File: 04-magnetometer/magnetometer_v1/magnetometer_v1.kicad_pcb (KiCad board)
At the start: 4 copper layers, 28.5 x 23.5 mm, 42 parts, among them IC1 STM32F072CBT6, IC2 TMAG5170A1QDGKR, IC3 TCAN1042GVDRQ1, J1 Conn_02x04_Odd_Even, J2 USB4110-GF-A, SW3 SW_SPDT, U1 SPX3819M5-L-3-3/TR, U2 NANOT100AS, U3 NANOT100AS

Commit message: clean up routing
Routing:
- net GND: track 75.3 -> 76.1 mm

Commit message: made review changes
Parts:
- moved R4 0.91 mm to (176.4, 64.2), turned to 180 degrees
- moved R8 0.30 mm to (178.0, 65.3)
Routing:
- net GND: track 76.1 -> 68.6 mm, vias 36 -> 33
- net USB_D+: track 12.1 -> 13.9 mm
- net CAN_STM: track 21.4 -> 19.8 mm
- net USB_D-: track 13.3 -> 14.4 mm
- net 5v: track 2.45 -> 3.20 mm
- net 3v3: track 51.9 -> 52.5 mm, vias 11 -> 10

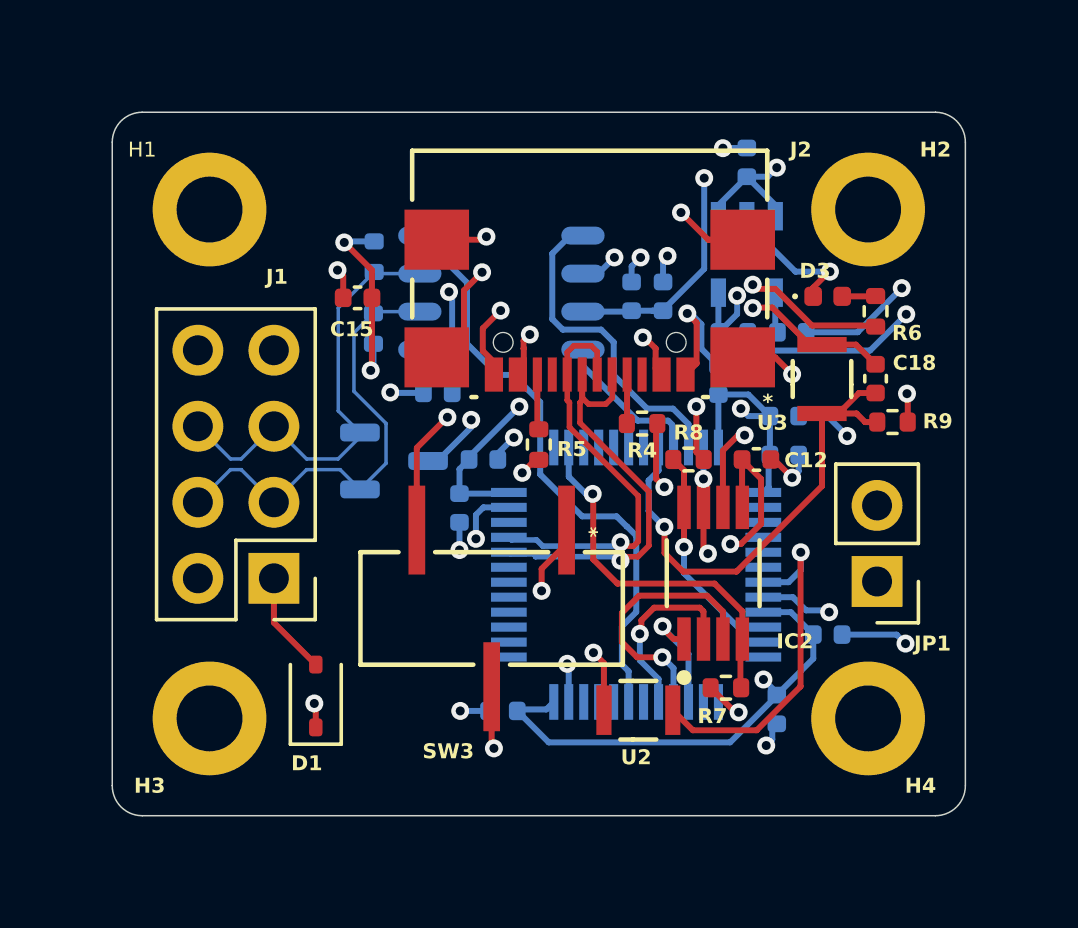
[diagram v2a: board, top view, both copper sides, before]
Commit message: update slide switch footprint
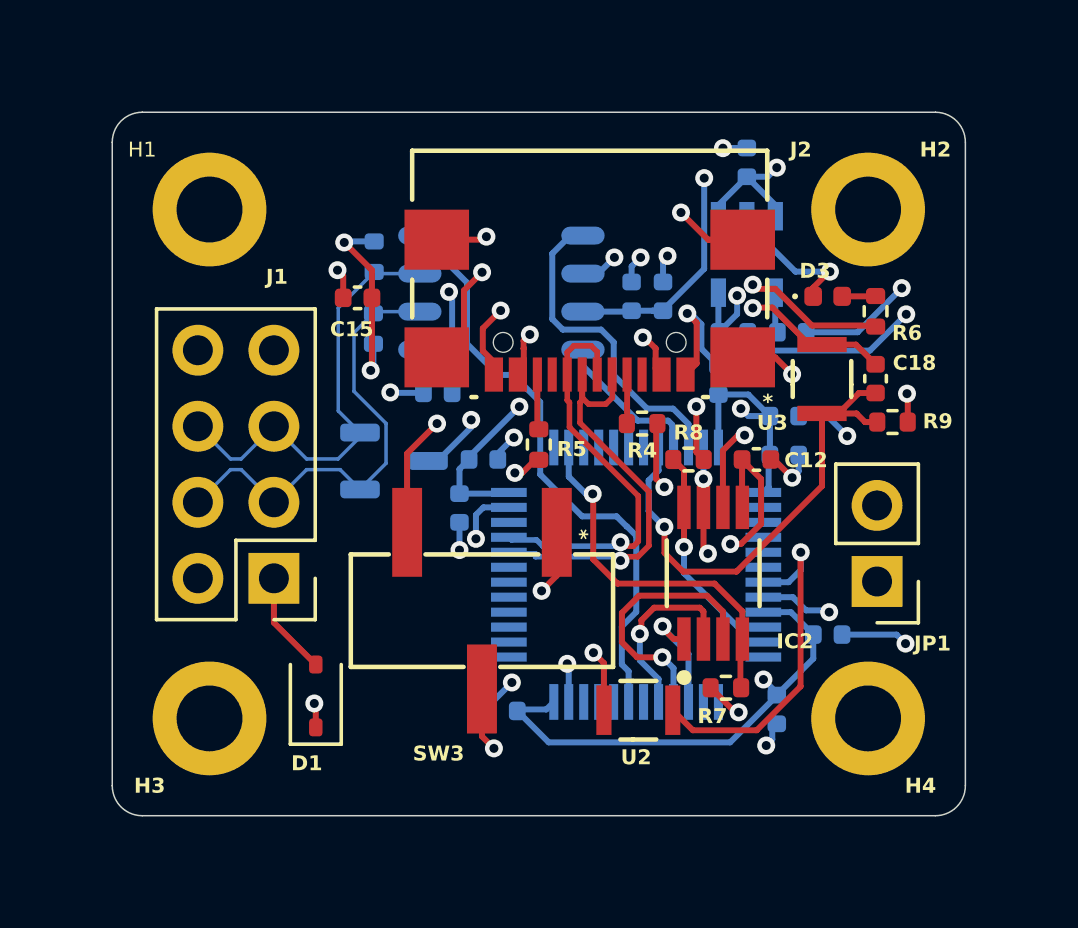
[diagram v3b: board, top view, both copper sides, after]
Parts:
- moved SW3 0.33 mm to (171.1, 70.4)
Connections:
- J2 pad 15: GND -> (no net)
- J2 pad 16: GND -> (no net)
- J2 pad 17: GND -> (no net)
- J2 pad 18: GND -> (no net)
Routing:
- net GND: track 68.6 -> 69.2 mm
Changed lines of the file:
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@@
 	(footprint "mag-fp:SW_JS102011SCQN"
 		(layer "F.Cu")
-		(at 171.425 70.325 -90)
+		(at 171.1 70.4 -90)
 		(tags "JS102011SCQN ")
 		(property "Reference" "SW3"
@@
 		(pad "1" smd rect
 			(at -2.6162 -2.5 270)
-			(size 2.9718 0.5588)
+			(size 2.9718 1)
 			(layers "F.Cu" "F.Mask" "F.Paste")
 			(net 8 "5v")
@@
 		(pad "2" smd rect
 			(at 2.6162 0 270)
-			(size 2.9718 0.5588)
+			(size 2.9718 1)
 			(layers "F.Cu" "F.Mask" "F.Paste")
 			(net 55 "VIN_JUMP")
@@
 		(pad "3" smd rect
 			(at -2.6162 2.5 270)
-			(size 2.9718 0.5588)
+			(size 2.9718 1)
 			(layers "F.Cu" "F.Mask" "F.Paste")
 			(net 52 "VBUS")
@@
 		)
 		(embedded_fonts no)
-		(model "${KICAD9_3DMODEL_DIR}/Package_TO_SOT_SMD.3dshapes/SuperSOT-3.step"
-			(offset
-				(xyz 0 0 0)
-			)
-			(scale
-				(xyz 2.6 2.7 1)
-			)
-			(rotate
-				(xyz -0 -0 -0)
-			)
-		)
 	)
 	(footprint "mag-fp:TMAG5170A2QDGKR"
@@
 			(size 2.159 2.0066)
 			(layers "F.Cu" "F.Mask" "F.Paste")
-			(net 2 "GND")
 		)
 		(pad "16" smd rect
@@
 			(size 2.159 2.0066)
 			(layers "F.Cu" "F.Mask" "F.Paste")
-			(net 2 "GND")
 		)
 		(pad "17" smd rect
@@
 			(size 2.159 2.0066)
 			(layers "F.Cu" "F.Mask" "F.Paste")
-			(net 2 "GND")
 		)
 		(pad "18" smd rect
@@
 			(size 2.159 2.0066)
 			(layers "F.Cu" "F.Mask" "F.Paste")
-			(net 2 "GND")
 		)
 		(pad "A1-B12" smd rect
@@
 	)
 	(segment
-		(start 173 65.36)
-		(end 172.881602 65.36)
+		(start 172.2 65.797597)
+		(end 172.444005 65.797597)
 		(width 0.2)
 		(layer "F.Cu")
@@
 	)
 	(segment
+		(start 172.881602 65.36)
+		(end 173 65.36)
+		(width 0.2)
+		(layer "F.Cu")
+		(net 2)
+	)
+	(segment
 		(start 180.855939 65.35)
 		(end 180.75 65.35)
@@
 	)
 	(segment
-		(start 172.881602 65.36)
-		(end 172.446601 65.795001)
-		(width 0.2)
-		(layer "F.Cu")
-		(net 2)
-	)
-	(segment
 		(start 176.919 64.191)
 		(end 176.919 65.995362)
@@
 	)
 	(segment
+		(start 172.444005 65.797597)
+		(end 172.881602 65.36)
+		(width 0.2)
+		(layer "F.Cu")
+		(net 2)
+	)
+	(segment
 		(start 178.65 68.4947)
 		(end 178.5 68.3447)
@@
 	)
 	(via
-		(at 172.446601 65.795001)
+		(at 172.2 65.797597)
 		(size 0.6)
 		(drill 0.3)
@@
 	)
 	(via
-		(at 170.375 73.75)
+		(at 172.1 72.8)
 		(size 0.6)
 		(drill 0.3)
@@
 	)
 	(segment
+		(start 171.320001 73.749999)
+		(end 171.320001 73.579999)
+		(width 0.2)
+		(layer "B.Cu")
+		(net 2)
+	)
+	(segment
 		(start 181.575 59.075)
 		(end 182.725 59.075)
@@
 	)
 	(segment
-		(start 171.320001 73.749999)
-		(end 170.375 73.75)
-		(width 0.2)
-		(layer "B.Cu")
-		(net 2)
-	)
-	(segment
 		(start 177.15 58.7)
 		(end 177.3 58.55)
@@
 	)
 	(segment
+		(start 171.320001 73.579999)
+		(end 172.1 72.8)
+		(width 0.2)
+		(layer "B.Cu")
+		(net 2)
+	)
+	(segment
 		(start 181.680001 63.899999)
 		(end 182.637336 63.899999)
@@
 	)
 	(segment
-		(start 173.925 68.171904)
-		(end 173.925 67.7088)
-		(width 0.2)
-		(layer "F.Cu")
-		(net 8)
-	)
-	(segment
-		(start 173.093454 69.738964)
-		(end 173.093454 69.00345)
+		(start 173.6 67.7838)
+		(end 173.6 69.232418)
 		(width 0.2)
 		(layer "F.Cu")
@@
 	)
 	(segment
-		(start 165.55 74.3)
-		(end 165.55 73.55)
+		(start 173.6 69.232418)
+		(end 173.093454 69.738964)
 		(width 0.2)
 		(layer "F.Cu")
@@
 	)
 	(segment
-		(start 173.093454 69.00345)
-		(end 173.925 68.171904)
+		(start 165.55 74.3)
+		(end 165.55 73.55)
 		(width 0.2)
 		(layer "F.Cu")
@@
 	)
 	(segment
-		(start 179.735 71.415001)
-		(end 179.8 71.350001)
+		(start 178.870699 69.4957)
+		(end 179.8 70.425001)
 		(width 0.2)
 		(layer "F.Cu")
@@
 	)
 	(segment
-		(start 175.62579 69.4957)
-		(end 174.818424 68.688334)
+		(start 174.8 66.5)
+		(end 174.818424 66.518424)
 		(width 0.2)
 		(layer "F.Cu")
@@
 	)
 	(segment
-		(start 174.818424 66.518424)
-		(end 174.8 66.5)
+		(start 175.62579 69.4957)
+		(end 178.870699 69.4957)
 		(width 0.2)
 		(layer "F.Cu")
@@
 	)
 	(segment
-		(start 179.8 70.425001)
-		(end 178.870699 69.4957)
+		(start 179.735 71.415001)
+		(end 179.8 71.350001)
 		(width 0.2)
 		(layer "F.Cu")
@@
 	)
 	(segment
-		(start 178.870699 69.4957)
-		(end 175.62579 69.4957)
+		(start 174.818424 66.518424)
+		(end 174.818424 68.688334)
 		(width 0.2)
 		(layer "F.Cu")
@@
 	)
 	(segment
-		(start 174.818424 68.688334)
-		(end 174.818424 66.518424)
+		(start 179.735 73.05)
+		(end 179.735 71.415001)
 		(width 0.2)
 		(layer "F.Cu")
@@
 	)
 	(segment
-		(start 179.735 73.05)
-		(end 179.735 71.415001)
+		(start 179.8 70.425001)
+		(end 179.8 71.350001)
 		(width 0.2)
 		(layer "F.Cu")
@@
 	)
 	(segment
-		(start 179.8 71.350001)
-		(end 179.8 70.425001)
+		(start 174.818424 68.688334)
+		(end 175.62579 69.4957)
 		(width 0.2)
 		(layer "F.Cu")
@@
 	)
 	(segment
-		(start 174.8 66.5)
-		(end 174.711433 66.5)
-		(width 0.2)
-		(layer "B.Cu")
-		(net 32)
-	)
-	(segment
 		(start 174.704398 66.507035)
 		(end 174.582035 66.507035)
@@
 	)
 	(segment
+		(start 174.8 66.5)
+		(end 174.711433 66.5)
+		(width 0.2)
+		(layer "B.Cu")
+		(net 32)
+	)
+	(segment
 		(start 177.453402 64.186689)
 		(end 177.453402 64.95)
@@
 	)
 	(segment
+		(start 168.6 67.7838)
+		(end 168.6 65.15)
+		(width 0.2)
+		(layer "F.Cu")
+		(net 52)
+	)
+	(segment
 		(start 176.538099 61.275)
 		(end 176.903399 61.6403)
@@
 	)
 	(segment
-		(start 172.491199 61.6403)
-		(end 172.491199 61.383801)
+		(start 168.6 65.15)
+		(end 169.6 64.15)
 		(width 0.2)
 		(layer "F.Cu")
@@
 	)
 	(segment
-		(start 168.925 64.961073)
-		(end 169.94584 63.940233)
+		(start 172.491199 61.6403)
+		(end 172.491199 61.383801)
 		(width 0.2)
 		(layer "F.Cu")
@@
 		(net 52)
 	)
-	(segment
-		(start 168.925 67.7088)
-		(end 168.925 64.961073)
-		(width 0.2)
-		(layer "F.Cu")
-		(net 52)
-	)
 	(via
 		(at 176.475 61.275)
@@
 	)
 	(via
-		(at 169.94584 63.940233)
+		(at 169.6 64.15)
 		(size 0.6)
 		(drill 0.3)
@@
 	)
 	(segment
-		(start 171.425 72.9412)
-		(end 171.425 74.925)
+		(start 171.1 74.6)
+		(end 171.5 75)
 		(width 0.2)
 		(layer "F.Cu")
@@
 	)
 	(segment
-		(start 171.425 74.925)
-		(end 171.5 75)
+		(start 171.1 73.0162)
+		(end 171.1 74.6)
 		(width 0.2)
 		(layer "F.Cu")
@@
 			(pts
 				(xy 158 53) (xy 168.75 53) (xy 168.75 65) (xy 171.75 65) (xy 171.75 63) (xy 177.75 63) (xy 177.77625 57.75)
-				(xy 180.6 57.75) (xy 180.6 74.25) (xy 173.75 74.25) (xy 173.75 69.75) (xy 173.75 69.75) (xy 173.75 68.25)
-				(xy 163.25 68.25) (xy 163.25 60) (xy 158 60)
+				(xy 180.6 57.75) (xy 180.6 74.25) (xy 173.75 74.25) (xy 173.75 69.75) (xy 173.75 68.25) (xy 163.25 68.25)
+				(xy 163.25 60) (xy 158 60)
 			)
 		)
@@
 		(polygon
 			(pts
-				(xy 172.5 74.5) (xy 172.5 74.5) (xy 171 74.5) (xy 171 78) (xy 187.5 78) (xy 187.5 68.25) (xy 180.75 68.25)
-				(xy 180.75 74.5)
+				(xy 172.5 74.5) (xy 171 74.5) (xy 171 78) (xy 187.5 78) (xy 187.5 68.25) (xy 180.75 68.25) (xy 180.75 74.5)
 			)
 		)

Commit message: minor changes
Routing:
- net GND: track 69.2 -> 70.5 mm, vias 33 -> 32
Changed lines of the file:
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@@
 		(fp_line
 			(start -2.0066 4.5085)
-			(end -2.0066 3.008)
+			(end -2.0066 3.1)
 			(stroke
 				(width 0.1524)
@@
 		)
 		(fp_line
-			(start -4.2545 3.008)
-			(end -4.2545 -3.008)
+			(start -4.2545 3.1)
+			(end -4.2545 -3.1)
 			(stroke
 				(width 0.1524)
@@
 		)
 		(fp_line
-			(start -2.0066 3.008)
-			(end -4.2545 3.008)
+			(start -2.0066 3.1)
+			(end -4.2545 3.1)
 			(stroke
 				(width 0.1524)
@@
 		)
 		(fp_line
-			(start 2.0066 3.008)
+			(start 2.0066 3.1)
 			(end 2.0066 4.5085)
 			(stroke
@@
 		)
 		(fp_line
-			(start 4.2545 3.008)
-			(end 2.0066 3.008)
+			(start 4.2545 3.1)
+			(end 2.0066 3.1)
 			(stroke
 				(width 0.1524)
@@
 		)
 		(fp_line
-			(start -4.2545 -3.008)
-			(end -2.0066 -3.008)
+			(start -4.2545 -3.1)
+			(end -2.0066 -3.1)
 			(stroke
 				(width 0.1524)
@@
 		)
 		(fp_line
-			(start -2.0066 -3.008)
+			(start -2.0066 -3.1)
 			(end -2.0066 -4.5085)
 			(stroke
@@
 		)
 		(fp_line
-			(start 2.0066 -3.008)
-			(end 4.2545 -3.008)
+			(start 2.0066 -3.1)
+			(end 4.2545 -3.1)
 			(stroke
 				(width 0.1524)
@@
 		)
 		(fp_line
-			(start 4.2545 -3.008)
-			(end 4.2545 3.008)
+			(start 4.2545 -3.1)
+			(end 4.2545 3.1)
 			(stroke
 				(width 0.1524)
@@
 		(fp_line
 			(start 2.0066 -4.5085)
-			(end 2.0066 -3.008)
+			(end 2.0066 -3.1)
 			(stroke
 				(width 0.1524)
@@
 	)
 	(via
-		(at 178.5 66)
-		(size 0.6)
-		(drill 0.3)
-		(layers "F.Cu" "B.Cu")
-		(net 2)
-	)
-	(via
 		(at 182.725 59.075)
 		(size 0.6)
@@
 	)
 	(segment
-		(start 178.5 65.905595)
-		(end 178.500002 65.905593)
+		(start 178.031438 66.269862)
+		(end 177.1935 66.269862)
 		(width 0.2)
 		(layer "B.Cu")
@@
 	)
 	(segment
-		(start 178.5 66)
-		(end 178.5 65.905595)
-		(width 0.2)
-		(layer "B.Cu")
-		(net 2)
-	)
-	(segment
 		(start 177.15 59.42)
 		(end 177.15 58.7)
@@
 	)
 	(segment
+		(start 178.500002 65.801298)
+		(end 178.031438 66.269862)
+		(width 0.2)
+		(layer "B.Cu")
+		(net 2)
+	)
+	(segment
 		(start 171.63 65.152832)
 		(end 172.166416 64.616416)
@@
 	)
 	(segment
-		(start 178.500002 65.905593)
-		(end 178.500002 64.95)
+		(start 178.500002 64.95)
+		(end 178.500002 65.801298)
 		(width 0.2)
 		(layer "B.Cu")
@@
 	)
 	(segment
-		(start 178.263217 63.580877)
-		(end 178.263217 65.103217)
-		(width 0.2)
-		(layer "F.Cu")
-		(net 4)
-	)
-	(segment
 		(start 182.0372 61.5122)
 		(end 180.8 60.275)
@@
 	)
 	(segment
+		(start 178.263217 63.580875)
+		(end 178.263217 65.103217)
+		(width 0.2)
+		(layer "F.Cu")
+		(net 4)
+	)
+	(segment
 		(start 180.425 67.5)
 		(end 180.425 66)
@@
 	)
 	(via
-		(at 178.263217 63.580877)
+		(at 178.263217 63.580875)
 		(size 0.6)
 		(drill 0.3)

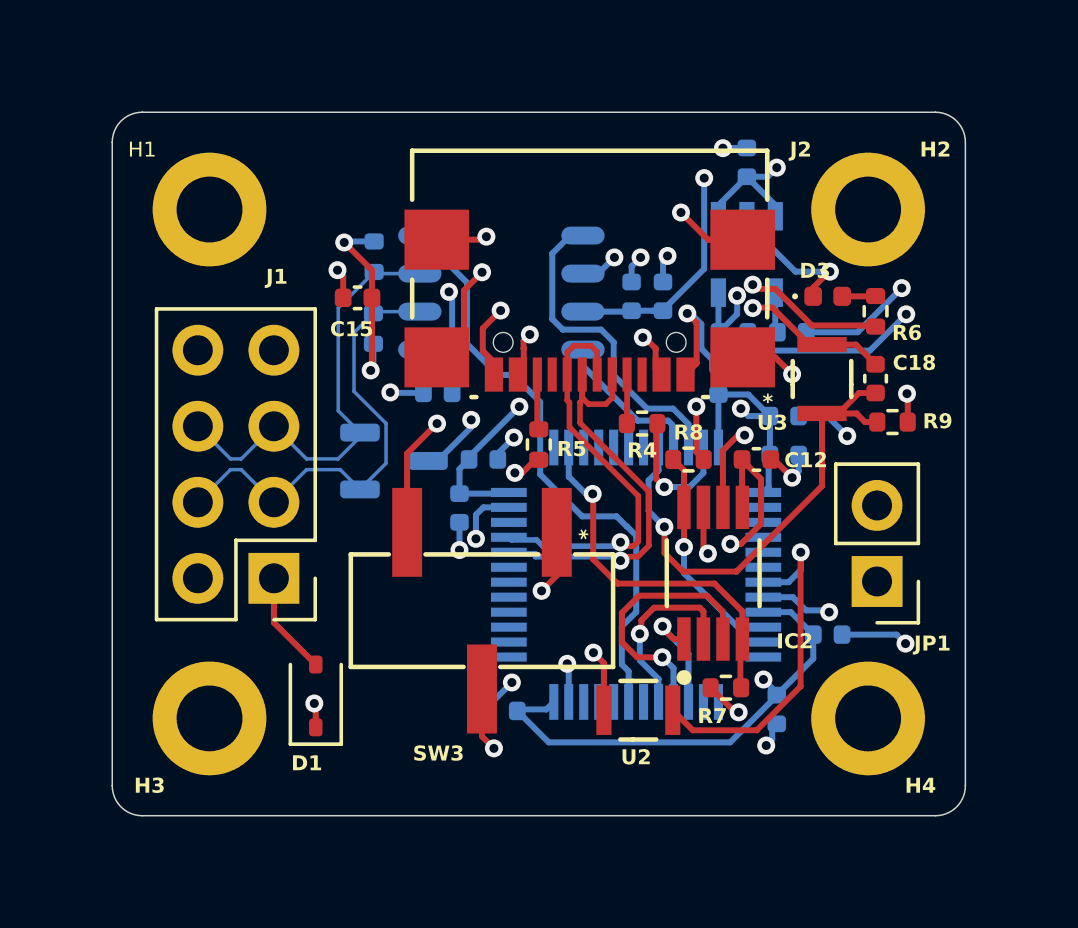
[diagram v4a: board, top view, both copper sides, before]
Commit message: fix via size
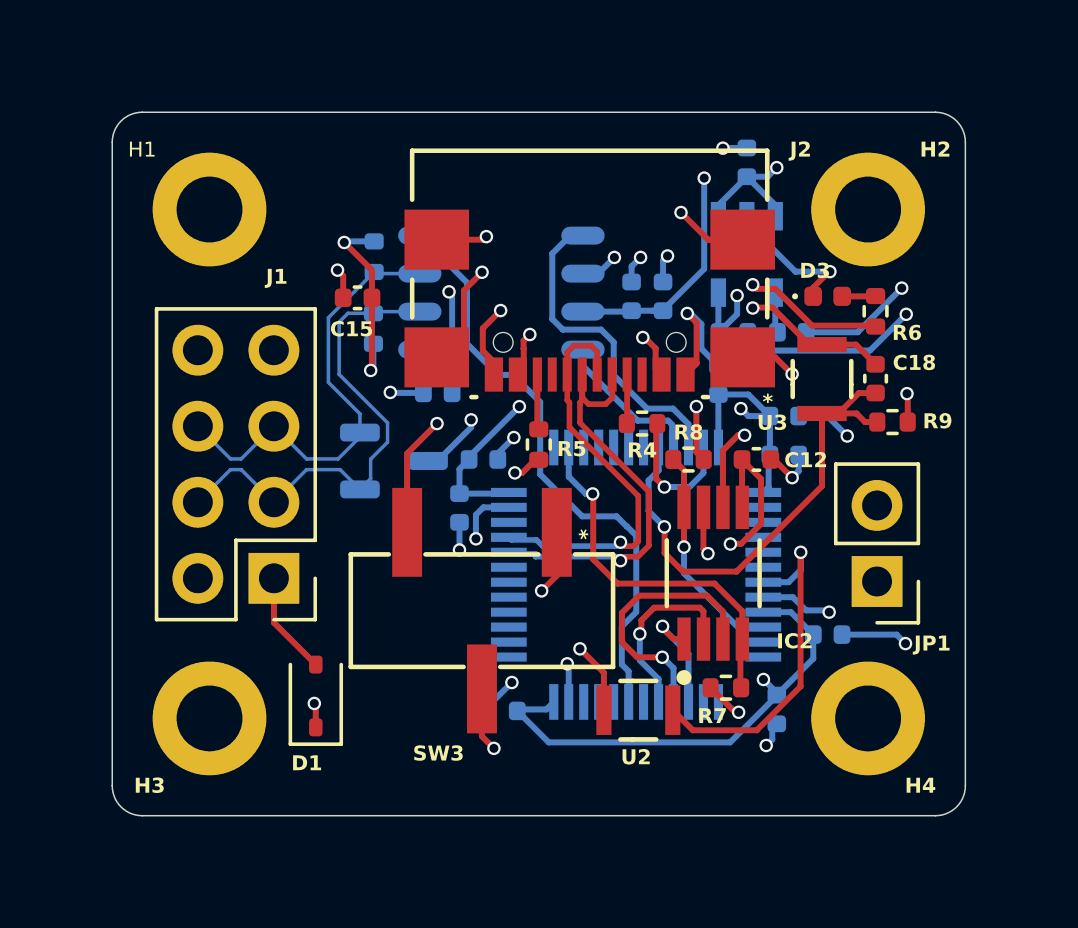
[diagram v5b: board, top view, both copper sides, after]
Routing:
- net CAN-: track 15.6 -> 16.5 mm
